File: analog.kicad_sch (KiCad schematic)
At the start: 45 parts, among them J8 Sensor harness

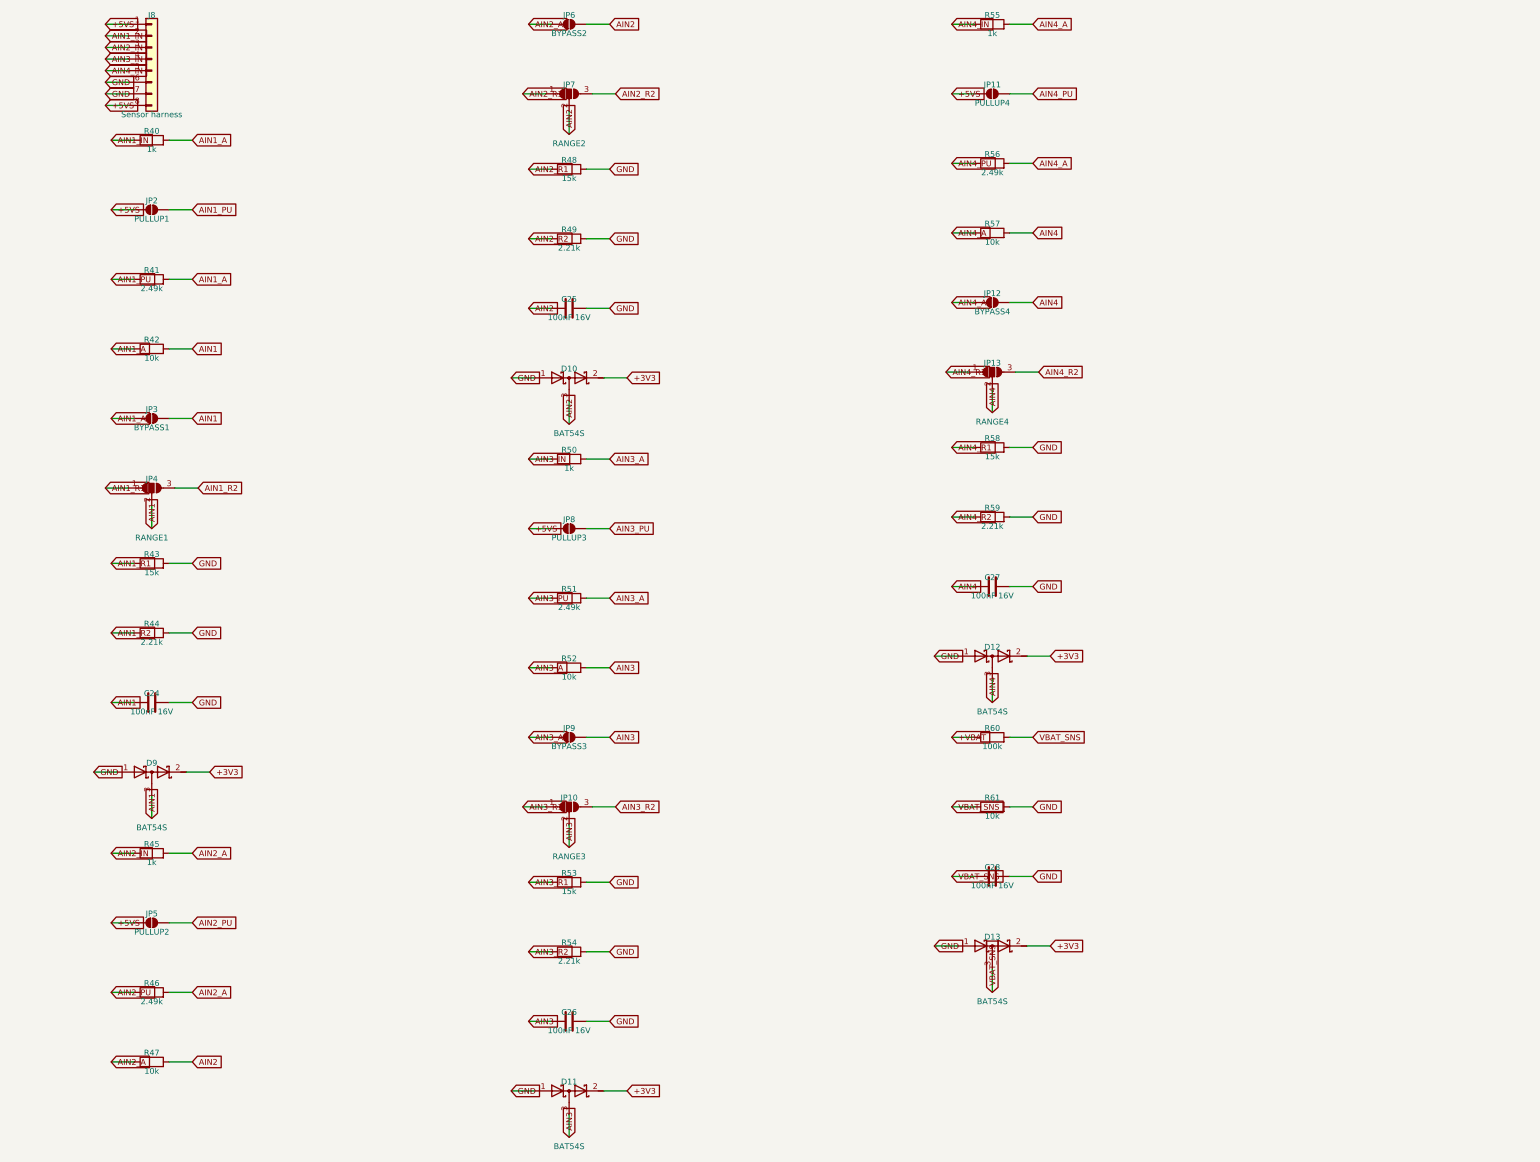
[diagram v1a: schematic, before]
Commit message: Fix the LM5164 power stages against the datasheet and TI's DDA drawing
Review of datasheet SNVSAU4D and package drawing 4214849/B (DDA0008B)
caught five issues, all fixed and re-verified:

- RON placeholders (100k -> ~125/83kHz) corrected to 31.6k (396kHz, 5V)
  and 20.5k (402kHz, 3V3); minimum on-time at the 53.3V clamp is
  237ns/154ns, well above the 50ns floor.
- Bootstrap caps were 100nF; the datasheet mandates exactly 2.2nF and
  warns larger values damage the internal VCC regulator. Now 2.2nF 50V.
- No FB ripple injection on the all-ceramic outputs -- a COT stability
  requirement (Table 6-1). Added Type-3 networks (RA/CA/CB: 121k and
  95.3k / 3.3nF / 270pF) sized for ~20mV ramp at 14V per TI's example.
- Exposed-pad footprint EP2.41x3.3mm was smaller than the DDA0008B pad
  itself (max 2.71x3.4mm); swapped to the EP2.95x4.9mm_Mask2.71x3.4mm
  footprint matching TI's example land pattern.
- Quantified BAT54S back-feed into +3V3: one input shorted to battery
  floats the rail to ~3.6V when the MCU sleeps. Added D2, an MM3Z3V6T1G
  3.6V zener rail clamp.

Load-dump assumption confirmed by the owner: alternator never exceeds
20V, so the SMCJ33A standoff has comfortable margin.

Validated with kicad-cli 9.0: 104 nets / 160 instances match, ERC clean.

Co-Authored-By: Claude Fable 5 <noreply@anthropic.com>
Claude-Session: https://claude.ai/code/session_01DhNbL25h25p8VFCjRfJik9
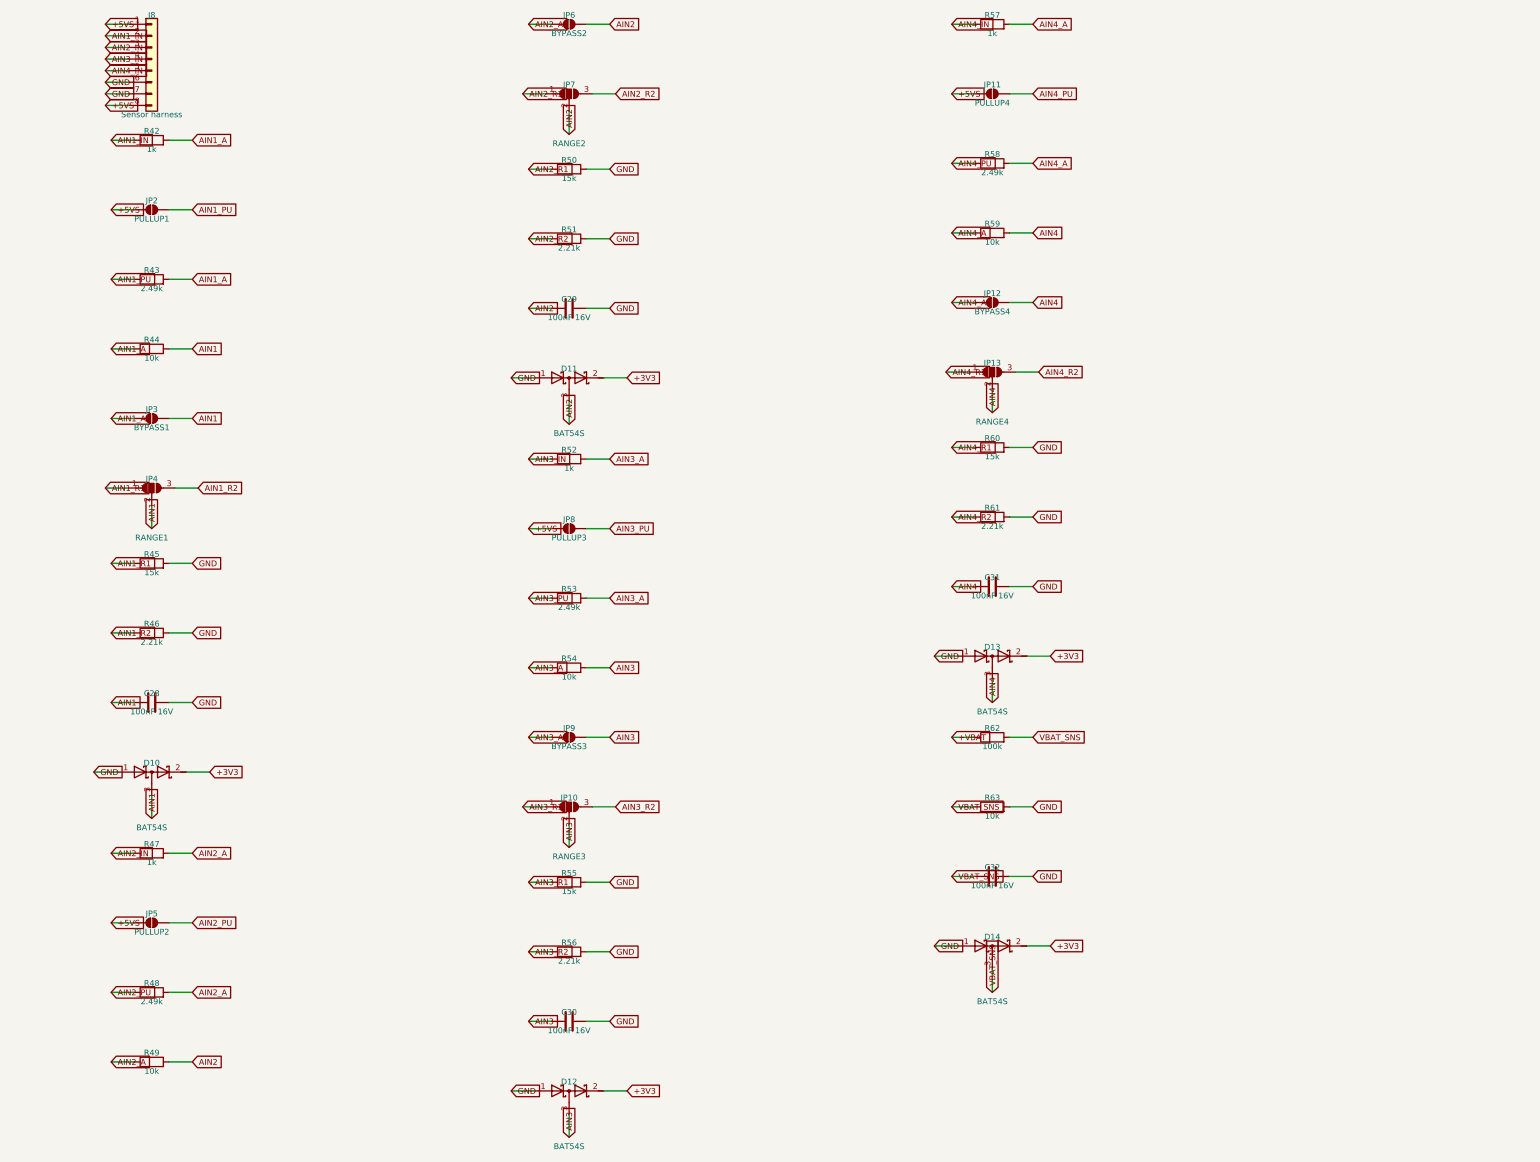
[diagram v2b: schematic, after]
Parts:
- removed C24, C25, C26, C27: 100nF 16V, Capacitor_SMD:C_0805_2012Metric, symbol Device:C
- removed D9: BAT54S, Package_TO_SOT_SMD:SOT-23, symbol Device:D_Schottky_Dual_Series_AKC
- removed R40: 1k, Resistor_SMD:R_0805_2012Metric, symbol Device:R
- removed R41: 2.49k, Resistor_SMD:R_0805_2012Metric, symbol Device:R
- added C29, C30, C31, C32: 100nF 16V, Capacitor_SMD:C_0805_2012Metric, symbol Device:C
- added D14: BAT54S, Package_TO_SOT_SMD:SOT-23, symbol Device:D_Schottky_Dual_Series_AKC
- added R62: 100k, Resistor_SMD:R_0805_2012Metric, symbol Device:R
- added R63: 10k, Resistor_SMD:R_0805_2012Metric, symbol Device:R
- C28: Note (none) -> Ch1 anti-alias / ADC charge reservoir
- D10: Note Ch2 rail clamp (both polarities) -> Ch1 rail clamp (both polarities)
- D11: Note Ch3 rail clamp (both polarities) -> Ch2 rail clamp (both polarities)
- D12: Note Ch4 rail clamp (both polarities) -> Ch3 rail clamp (both polarities)
- D13: Note Battery-monitor clamp -> Ch4 rail clamp (both polarities)
- R42: value 10k -> 1k; Note Ch1 divider upper leg -> Ch1 series/fault-current limit
- R43: value 15k -> 2.49k; Note 0-5V range: 5.0V in -> 3.00V at the ADC -> Ch1 bias resistor
- R44: value 2.21k -> 10k; Note 0-16V range: 16.0V in -> 2.89V at the ADC -> Ch1 divider upper leg
- R45: value 1k -> 15k; Note Ch2 series/fault-current limit -> 0-5V range: 5.0V in -> 3.00V at the ADC
- R46: value 2.49k -> 2.21k; Note Ch2 bias resistor -> 0-16V range: 16.0V in -> 2.89V at the ADC
- R47: value 10k -> 1k; Note Ch2 divider upper leg -> Ch2 series/fault-current limit
- R48: value 15k -> 2.49k; Note 0-5V range: 5.0V in -> 3.00V at the ADC -> Ch2 bias resistor
- R49: value 2.21k -> 10k; Note 0-16V range: 16.0V in -> 2.89V at the ADC -> Ch2 divider upper leg
- R50: value 1k -> 15k; Note Ch3 series/fault-current limit -> 0-5V range: 5.0V in -> 3.00V at the ADC
- R51: value 2.49k -> 2.21k; Note Ch3 bias resistor -> 0-16V range: 16.0V in -> 2.89V at the ADC
- R52: value 10k -> 1k; Note Ch3 divider upper leg -> Ch3 series/fault-current limit
- R53: value 15k -> 2.49k; Note 0-5V range: 5.0V in -> 3.00V at the ADC -> Ch3 bias resistor
- R54: value 2.21k -> 10k; Note 0-16V range: 16.0V in -> 2.89V at the ADC -> Ch3 divider upper leg
- R55: value 1k -> 15k; Note Ch4 series/fault-current limit -> 0-5V range: 5.0V in -> 3.00V at the ADC
- R56: value 2.49k -> 2.21k; Note Ch4 bias resistor -> 0-16V range: 16.0V in -> 2.89V at the ADC
- R57: value 10k -> 1k; Note Ch4 divider upper leg -> Ch4 series/fault-current limit
- R58: value 15k -> 2.49k; Note 0-5V range: 5.0V in -> 3.00V at the ADC -> Ch4 bias resistor
- R59: value 2.21k -> 10k; Note 0-16V range: 16.0V in -> 2.89V at the ADC -> Ch4 divider upper leg
- R60: value 100k -> 15k; Note Battery monitor: divide by 11 -> 0-5V range: 5.0V in -> 3.00V at the ADC
- R61: value 10k -> 2.21k; Note (none) -> 0-16V range: 16.0V in -> 2.89V at the ADC
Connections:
- net +3V3: now also D14.2 (K)
- net +VBAT: now also R62.1; no longer R60.1
- net AIN1: now also C28.1, D10.3 (common), R44.2; no longer R42.2
- net AIN1_A: now also R42.2, R43.2, R44.1; no longer R42.1
- net AIN1_IN: now also R42.1
- net AIN1_PU: now also R43.1
- net AIN1_R1: now also R45.1; no longer R43.1
- net AIN1_R2: now also R46.1; no longer R44.1
- net AIN2: now also D11.3 (common), R49.2, C29.1; no longer D10.3 (common), R47.2
- net AIN2_A: now also R47.2, R48.2, R49.1; no longer R45.2, R46.2, R47.1
- net AIN2_IN: now also R47.1; no longer R45.1
- net AIN2_PU: now also R48.1; no longer R46.1
- net AIN2_R1: now also R50.1; no longer R48.1
- net AIN2_R2: now also R51.1; no longer R49.1
- net AIN3: now also D12.3 (common), R54.2, C30.1; no longer D11.3 (common), R52.2
- net AIN3_A: now also R52.2, R53.2, R54.1; no longer R50.2, R51.2, R52.1
- net AIN3_IN: now also R52.1; no longer R50.1
- net AIN3_PU: now also R53.1; no longer R51.1
- net AIN3_R1: now also R55.1; no longer R53.1
- net AIN3_R2: now also R56.1; no longer R54.1
- net AIN4: now also D13.3 (common), R59.2, C31.1; no longer D12.3 (common), R57.2
- net AIN4_A: now also R57.2, R58.2, R59.1; no longer R55.2, R56.2, R57.1
- net AIN4_IN: now also R57.1; no longer R55.1
- net AIN4_PU: now also R58.1; no longer R56.1
- net AIN4_R1: now also R60.1; no longer R58.1
- net AIN4_R2: now also R61.1; no longer R59.1
- net GND: now also R45.2, R46.2, R50.2, R51.2, R55.2, R56.2, R60.2, C29.2, C30.2, C31.2, C32.2, D14.1 (A), R63.2; no longer R43.2, R44.2, R48.2, R49.2, R53.2, R54.2, R58.2, R59.2
- net VBAT_SNS: now also C32.1, D14.3 (common), R62.2, R63.1; no longer C28.1, D13.3 (common), R60.2, R61.1
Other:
- moved on the sheet: C28, D10, D11, D12, D13, R42, R43, R44, R45, R46, R47, R48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

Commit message: Add an ADS1115-Q1 precision path for AFR logging
The board's mission now includes wideband AFR, and the ESP32-S3 ADC's
±1-2% (±0.2 AFR on a 0-5V output) is not tuning-grade. U7, an ADS1115-Q1
16-bit delta-sigma on the existing I2C bus at 0x48, shares the four
conditioned AINx nodes so firmware can choose per channel between the
fast internal ADC and the accurate external one. Inputs stay inside the
ADS1115 absolute maximum thanks to the existing BAT54S clamps.

The front end is upgraded to match: the divider resistors (1k series,
10k upper, 15k and 2.21k range legs) are now 0.1% thin-film, and the
range notes are corrected to include the 1k series resistor in the
divider math (5.0V in reads ~2.88V, not 3.00V; the exact scale is a
firmware calibration constant).

Validated with kicad-cli 9.0: 104 nets / 162 instances match, ERC clean.

Co-Authored-By: Claude Fable 5 <noreply@anthropic.com>
Claude-Session: https://claude.ai/code/session_01DhNbL25h25p8VFCjRfJik9
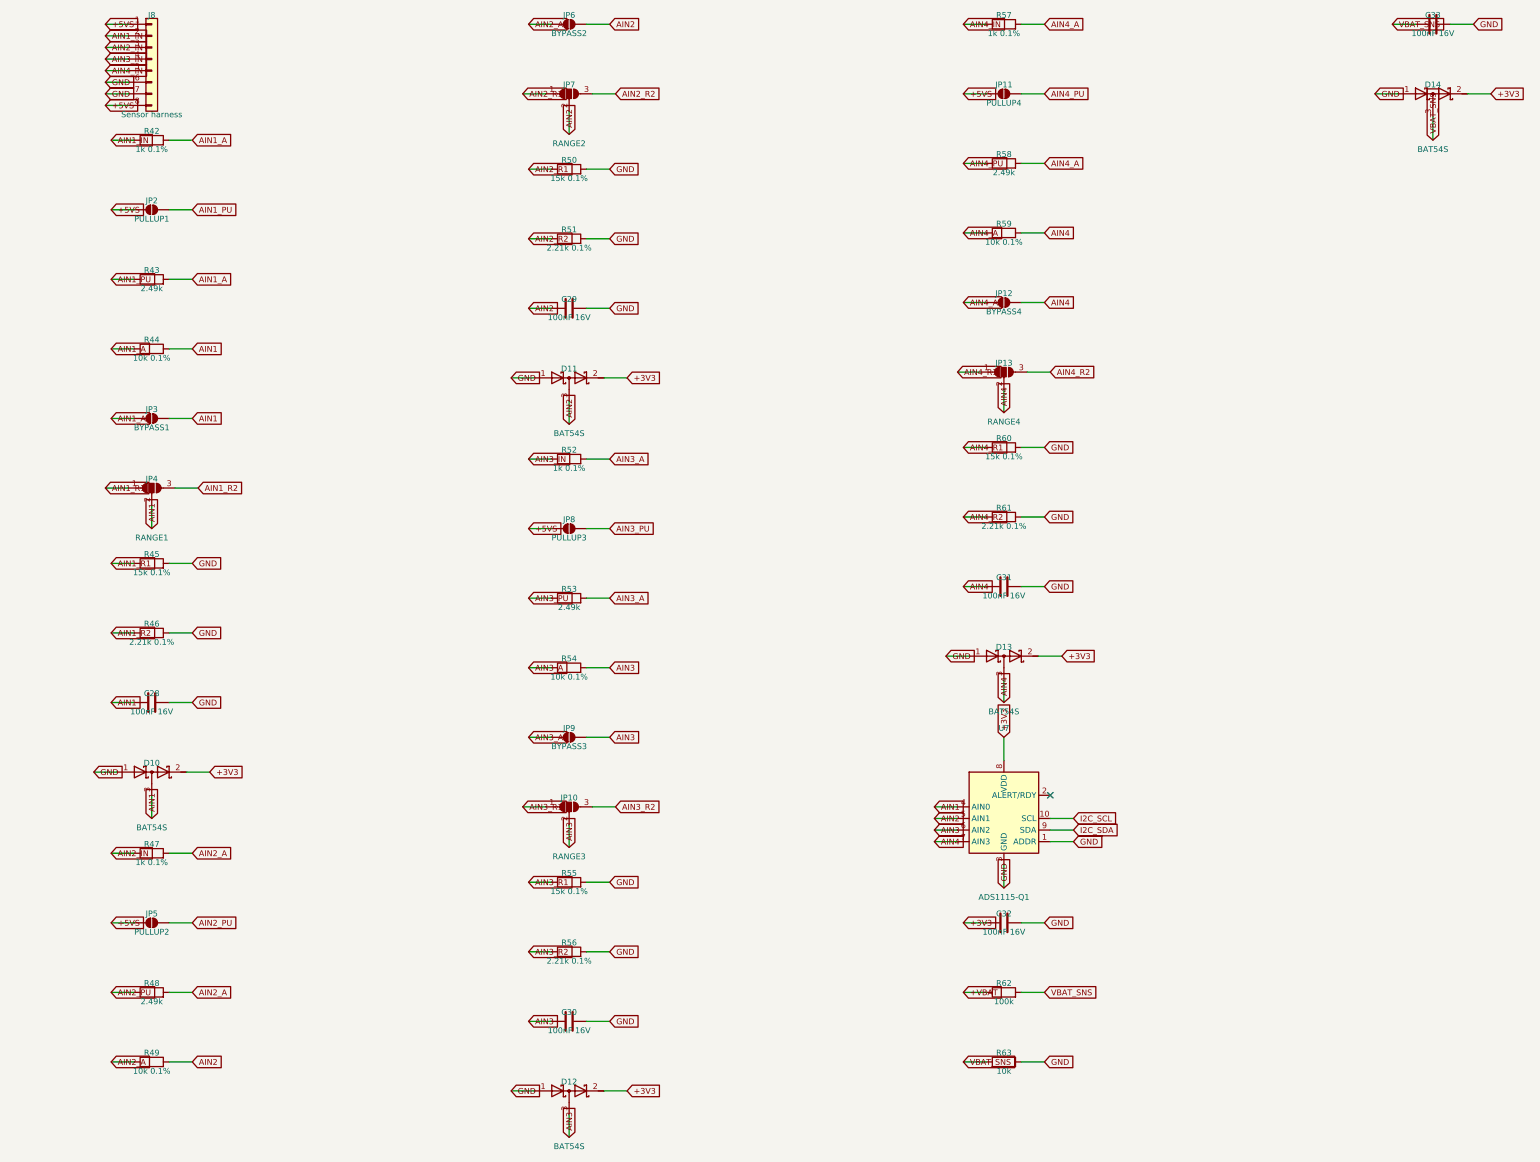
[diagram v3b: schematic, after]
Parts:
- added C33: 100nF 16V, Capacitor_SMD:C_0805_2012Metric, symbol Device:C
- added U7: ADS1115-Q1, Package_SO:VSSOP-10_3x3mm_P0.5mm, symbol Analog_ADC:ADS1115IDGS
- C32: Note (none) -> ADS1115 decoupling
- R42: value 1k -> 1k 0.1%; Note Ch1 series/fault-current limit -> Ch1 series/fault-current limit; 0.1% thin film -- it is ins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
- R44: value 10k -> 10k 0.1%; Note Ch1 divider upper leg -> Ch1 divider upper leg, 0.1% thin film for AFR-grade accuracy
- R45, R50, R55, R60: value 15k -> 15k 0.1%; Note 0-5V range: 5.0V in -> 3.00V at the ADC -> 0-5V range: 5.0V in -> ~2.88V at the ADC (1k series include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
- R46, R51, R56, R61: value 2.21k -> 2.21k 0.1%; Note 0-16V range: 16.0V in -> 2.89V at the ADC -> 0-16V range: 16.0V in -> ~2.67V at the ADC (1k series inclu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
- R47: value 1k -> 1k 0.1%; Note Ch2 series/fault-current limit -> Ch2 series/fault-current limit; 0.1% thin film -- it is ins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
- R49: value 10k -> 10k 0.1%; Note Ch2 divider upper leg -> Ch2 divider upper leg, 0.1% thin film for AFR-grade accuracy
- R52: value 1k -> 1k 0.1%; Note Ch3 series/fault-current limit -> Ch3 series/fault-current limit; 0.1% thin film -- it is ins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
- R54: value 10k -> 10k 0.1%; Note Ch3 divider upper leg -> Ch3 divider upper leg, 0.1% thin film for AFR-grade accuracy
- R57: value 1k -> 1k 0.1%; Note Ch4 series/fault-current limit -> Ch4 series/fault-current limit; 0.1% thin film -- it is ins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
- R59: value 10k -> 10k 0.1%; Note Ch4 divider upper leg -> Ch4 divider upper leg, 0.1% thin film for AFR-grade accuracy
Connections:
- net +3V3: now also C32.1, U7.8 (VDD)
- net AIN1: now also U7.4 (AIN0)
- net AIN2: now also U7.5 (AIN1)
- net AIN3: now also U7.6 (AIN2)
- net AIN4: now also U7.7 (AIN3)
- net GND: now also C33.2, U7.1 (ADDR), U7.3 (GND)
- net VBAT_SNS: now also C33.1; no longer C32.1
- new net I2C_SCL: U7.10 (SCL)
- new net I2C_SDA: U7.9 (SDA)
- no-connect marks 0 -> 1
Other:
- moved on the sheet: C31, C32, D13, D14, JP11, JP12, JP13, R57, R58, R59, R60, R61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
